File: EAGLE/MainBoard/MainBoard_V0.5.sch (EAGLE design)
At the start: 34 parts, among them IC2 CEM3340

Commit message: Renumber Parts
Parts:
- removed IC2: CEM3340, CEM:CEM3340
- removed J3: (no value), SparkFun-Connectors:CONN_08X2_SHROUD
- removed LINEAR-FM, PWM_C: WQP-PJ301M-12_JACK, thonkiconn:WQP-PJ301M-12_JACK
- removed R17: 20K, bourns:3386-W
- removed R18: 10K, bourns:3386-W
- removed R19, R20: 100K, rcl:R-US_0207/10
- added IC1: CEM3340, CEM:CEM3340
- added J8: (no value), SparkFun-Connectors:CONN_08X2_SHROUD
- added LIN_FM, PWM: WQP-PJ301M-12_JACK, thonkiconn:WQP-PJ301M-12_JACK
- added R13: 24KΩ, rcl:R-US_0207/10
- added R14: 1.8KΩ, rcl:R-US_0207/10
- added R5: 1MΩ, rcl:R-US_0207/10
- added R8: 10KΩ, rcl:R-US_0207/10
- C1, C3: value 0.01μF -> 0.001μF
- C4: value 1000pF -> 0.01μF
- C6: value 0.001μF -> 0.01μF
- CV2: SPICEPREFIX U -> (none)
- R1: value 1.8K -> 360KΩ
- R10: value 5.6K -> 5.6KΩ
- R11: value 600 -> 20KΩ; device rcl:R-US_0207/10 -> bourns:3386-W
- R12: value 10K -> 10KΩ; device rcl:R-US_0207/10 -> bourns:3386-W
- R15: value 470 -> 1.5MΩ
- R16: value 100K -> 470Ω
- R2: value 1.5M -> 100KΩ
- R3: value 360K -> 100KΩ
- R4: value 1M -> 100KΩ
- R6: value 1M -> 470Ω
- R7: value 470 -> 1MΩ
- R9: value 24K -> 600Ω
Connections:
- net +12V: now also IC1.16, J8.10, J8.9, R1.1, R15.1; no longer IC2.16, J3.10, J3.9, R2.1, R3.1
- net +5V: now also J8.11, J8.12; no longer J3.11, J3.12
- net -12V: now also J8.1, J8.2, R9.1; no longer J3.1, J3.2, R11.1
- net CV: now also J8.13, J8.14; no longer J3.13, J3.14
- net FCTL: now also IC1.15, R1.2, R2.1, R4.2, R6.1, R7.1; no longer IC2.15, R15.1, R16.1, R19.2, R20.2, R4.1
- net GATE: now also J8.15, J8.16; no longer J3.15, J3.16
- net GND: now also C5.2, C6.2, IC1.12, J8.3, J8.4, J8.5, J8.6, J8.7, J8.8, LIN_FM.1, PWM.1, R11.3, R14.1, R8.1; no longer C1.2, C3.2, IC2.12, J3.3, J3.4, J3.5, J3.6, J3.7, J3.8, LINEAR-FM.1, PWM_C.1, R1.1, R12.1, R17.3
- net HARD_S: now also C1.2, IC1.6; no longer C6.2, IC2.6
- net LIN_FM: now also IC1.13, R15.2, R16.1, R5.2; no longer IC2.13, R2.2, R6.2, R7.1
- net N$1: now also IC1.2; no longer IC2.2
- net N$10: now also R11.2, R7.2; no longer R17.2, R4.2
- net N$11: now also R12.3, R13.1; no longer R18.3, R9.1
- net N$13: now also IC1.7, R11.1; no longer IC2.7, R17.1
- net N$14: now also R2.2; no longer R16.2
- net N$15: now also IC1.3, R12.1, R12.2, R9.2; no longer IC2.3, R11.2, R18.1, R18.2
- net N$16: now also C1.1; no longer C6.1
- net N$2: now also C4.1, R6.2; no longer C1.1, R15.2
- net N$20: now also R3.1; no longer R19.1
- net N$22: now also R4.1; no longer R20.1
- net N$29: now also C3.2; no longer C5.2
- net N$3: now also IC1.14, R14.2; no longer IC2.14, R1.2
- net N$4: now also LIN_FM.2; no longer LINEAR-FM.2
- net N$5: now also R5.1; no longer R6.1
- net N$6: now also C6.1, R16.2; no longer C3.1, R7.2
- net N$7: now also C5.1, IC1.11; no longer C4.1, IC2.11
- net N$8: now also IC1.1, R13.2; no longer IC2.1, R9.2
- net PWM: now also IC1.5, PWM.2; no longer IC2.5, PWM_C.2
- net SAW: now also IC1.8; no longer IC2.8
- net SOFT_S: now also C3.1, IC1.9; no longer C5.1, IC2.9
- net SQUARE: now also IC1.4, R8.2; no longer IC2.4, R12.2
- net TRI: now also IC1.10; no longer IC2.10
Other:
- moved on the sheet: C1, C2, C3, C4, C5, C6, CV1, CV2, CV3, HARD_S, R1, R10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

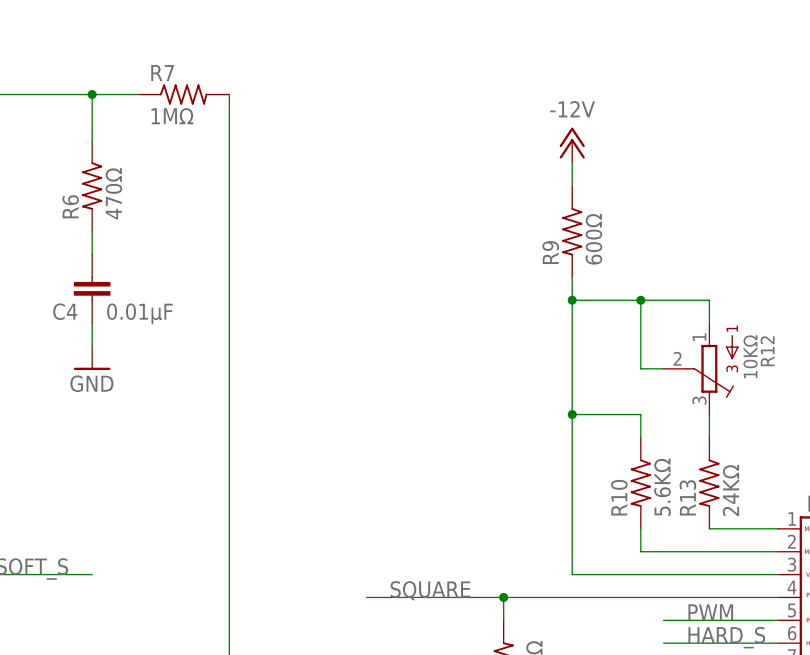
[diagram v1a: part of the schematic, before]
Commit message: Add 5V Reg. CAM Files
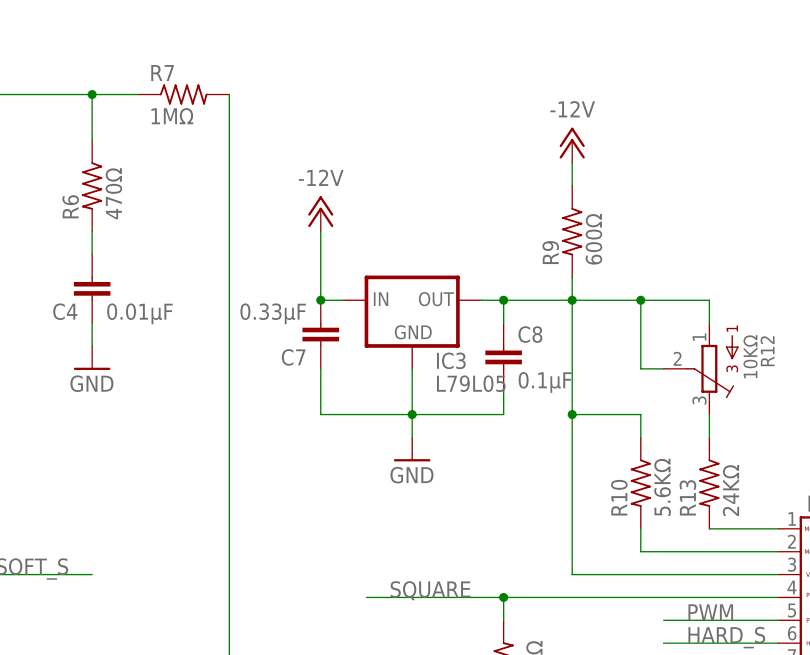
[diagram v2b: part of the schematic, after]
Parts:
- added C7: 0.33μF, rcl:C-EU050-025X075
- added C8: 0.1μF, rcl:C-EU050-025X075
- added IC3: L79L05, SparkFun-IC-Power:V_REG_78XXTO-92_UNTESTED
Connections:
- net -12V: now also C7.2, IC3.IN
- net GND: now also C7.1, C8.2, IC3.GND
- net N$15: now also C8.1, IC3.OUT
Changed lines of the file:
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@@
 <part name="CV2" library="thonkiconn" deviceset="WQP-PJ301M-12_JACK" device=""/>
 <part name="FRAME1" library="frames" library_urn="urn:adsk.eagle:library:229" deviceset="LETTER_L" device=""/>
+<part name="IC3" library="SparkFun-IC-Power" deviceset="V_REG_78XX" device="TO-92_UNTESTED" value="L79L05"/>
+<part name="P-4" library="supply1" library_urn="urn:adsk.eagle:library:371" deviceset="-12V" device=""/>
+<part name="C8" library="rcl" library_urn="urn:adsk.eagle:library:334" deviceset="C-EU" device="050-025X075" package3d_urn="urn:adsk.eagle:package:23637/1" value="0.1μF"/>
+<part name="C7" library="rcl" library_urn="urn:adsk.eagle:library:334" deviceset="C-EU" device="050-025X075" package3d_urn="urn:adsk.eagle:package:23637/1" value="0.33μF"/>
+<part name="GND18" library="supply1" library_urn="urn:adsk.eagle:library:371" deviceset="GND" device=""/>
 </parts>
 <sheets>
@@
 <attribute name="SHEET" x="233.68" y="1.27" size="2.54" layer="94"/>
 <attribute name="DRAWING_NAME" x="165.1" y="19.05" size="2.54" layer="94"/>
+</instance>
+<instance part="IC3" gate="G$1" x="111.76" y="124.46" smashed="yes">
+<attribute name="NAME" x="114.3" y="116.84" size="1.778" layer="95"/>
+<attribute name="VALUE" x="114.3" y="114.3" size="1.778" layer="96"/>
+</instance>
+<instance part="P-4" gate="1" x="101.6" y="134.62" smashed="yes" rot="R180">
+<attribute name="VALUE" x="99.06" y="137.16" size="1.778" layer="96"/>
+</instance>
+<instance part="C8" gate="G$1" x="121.92" y="119.38" smashed="yes">
+<attribute name="NAME" x="123.444" y="119.761" size="1.778" layer="95"/>
+<attribute name="VALUE" x="123.444" y="114.681" size="1.778" layer="96"/>
+</instance>
+<instance part="C7" gate="G$1" x="101.6" y="119.38" smashed="yes" rot="R180">
+<attribute name="NAME" x="100.076" y="118.999" size="1.778" layer="95" rot="R180"/>
+<attribute name="VALUE" x="100.076" y="124.079" size="1.778" layer="96" rot="R180"/>
+</instance>
+<instance part="GND18" gate="1" x="111.76" y="106.68" smashed="yes">
+<attribute name="VALUE" x="109.22" y="104.14" size="1.778" layer="96"/>
 </instance>
 </instances>
@@
 <pinref part="P-2" gate="1" pin="-12V"/>
 <wire x1="119.38" y1="22.86" x2="119.38" y2="25.4" width="0.1524" layer="91"/>
+</segment>
+<segment>
+<pinref part="P-4" gate="1" pin="-12V"/>
+<wire x1="101.6" y1="132.08" x2="101.6" y2="124.46" width="0.1524" layer="91"/>
+<pinref part="IC3" gate="G$1" pin="IN"/>
+<wire x1="101.6" y1="124.46" x2="104.14" y2="124.46" width="0.1524" layer="91"/>
+<pinref part="C7" gate="G$1" pin="2"/>
+<junction x="101.6" y="124.46"/>
 </segment>
 </net>
@@
 <wire x1="33.02" y1="127" x2="45.72" y2="127" width="0.1524" layer="91"/>
 </segment>
+<segment>
+<pinref part="IC3" gate="G$1" pin="GND"/>
+<wire x1="111.76" y1="116.84" x2="111.76" y2="111.76" width="0.1524" layer="91"/>
+<wire x1="101.6" y1="111.76" x2="111.76" y2="111.76" width="0.1524" layer="91"/>
+<wire x1="111.76" y1="111.76" x2="121.92" y2="111.76" width="0.1524" layer="91"/>
+<junction x="111.76" y="111.76"/>
+<pinref part="C8" gate="G$1" pin="2"/>
+<wire x1="121.92" y1="111.76" x2="121.92" y2="114.3" width="0.1524" layer="91"/>
+<pinref part="GND18" gate="1" pin="GND"/>
+<wire x1="111.76" y1="111.76" x2="111.76" y2="109.22" width="0.1524" layer="91"/>
+<pinref part="C7" gate="G$1" pin="1"/>
+<wire x1="101.6" y1="116.84" x2="101.6" y2="111.76" width="0.1524" layer="91"/>
+</segment>
 </net>
 <net name="N$16" class="0">
@@
 <pinref part="R12" gate="G$1" pin="2"/>
 <junction x="129.54" y="111.76"/>
-</segment>
-</net>
+<pinref part="IC3" gate="G$1" pin="OUT"/>
+<wire x1="119.38" y1="124.46" x2="121.92" y2="124.46" width="0.1524" layer="91"/>
+<pinref part="C8" gate="G$1" pin="1"/>
+<wire x1="121.92" y1="124.46" x2="129.54" y2="124.46" width="0.1524" layer="91"/>
+<wire x1="121.92" y1="121.92" x2="121.92" y2="124.46" width="0.1524" layer="91"/>
+<junction x="121.92" y="124.46"/>
+</segment>
+</net>

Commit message: Update Power IC Add Optional Component Clarification
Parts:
- IC3: device SparkFun-IC-Power:V_REG_78XXTO-92_UNTESTED -> SparkFun-IC-Power:V_REG_79LXX
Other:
- note added: "Place only R9 OR IC3, C7, & C8"
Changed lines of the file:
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@@
 <part name="CV2" library="thonkiconn" deviceset="WQP-PJ301M-12_JACK" device=""/>
 <part name="FRAME1" library="frames" library_urn="urn:adsk.eagle:library:229" deviceset="LETTER_L" device=""/>
-<part name="IC3" library="SparkFun-IC-Power" deviceset="V_REG_78XX" device="TO-92_UNTESTED" value="L79L05"/>
 <part name="P-4" library="supply1" library_urn="urn:adsk.eagle:library:371" deviceset="-12V" device=""/>
 <part name="C8" library="rcl" library_urn="urn:adsk.eagle:library:334" deviceset="C-EU" device="050-025X075" package3d_urn="urn:adsk.eagle:package:23637/1" value="0.1μF"/>
 <part name="C7" library="rcl" library_urn="urn:adsk.eagle:library:334" deviceset="C-EU" device="050-025X075" package3d_urn="urn:adsk.eagle:package:23637/1" value="0.33μF"/>
 <part name="GND18" library="supply1" library_urn="urn:adsk.eagle:library:371" deviceset="GND" device=""/>
+<part name="IC3" library="SparkFun-IC-Power" deviceset="V_REG_79LXX" device="" value="L79L05"/>
 </parts>
 <sheets>
 <sheet>
 <plain>
+<text x="114.3" y="134.62" size="1.778" layer="91" align="center">Place only R9
+OR
+IC3, C7, &amp; C8</text>
 </plain>
 <instances>
@@
 <attribute name="DRAWING_NAME" x="165.1" y="19.05" size="2.54" layer="94"/>
 </instance>
+<instance part="P-4" gate="1" x="101.6" y="134.62" smashed="yes" rot="R180">
+<attribute name="VALUE" x="99.06" y="137.16" size="1.778" layer="96"/>
+</instance>
+<instance part="C8" gate="G$1" x="121.92" y="119.38" smashed="yes">
+<attribute name="NAME" x="123.444" y="119.761" size="1.778" layer="95"/>
+<attribute name="VALUE" x="123.444" y="114.681" size="1.778" layer="96"/>
+</instance>
+<instance part="C7" gate="G$1" x="101.6" y="119.38" smashed="yes" rot="R180">
+<attribute name="NAME" x="100.076" y="118.999" size="1.778" layer="95" rot="R180"/>
+<attribute name="VALUE" x="100.076" y="124.079" size="1.778" layer="96" rot="R180"/>
+</instance>
+<instance part="GND18" gate="1" x="111.76" y="106.68" smashed="yes">
+<attribute name="VALUE" x="109.22" y="104.14" size="1.778" layer="96"/>
+</instance>
 <instance part="IC3" gate="G$1" x="111.76" y="124.46" smashed="yes">
 <attribute name="NAME" x="114.3" y="116.84" size="1.778" layer="95"/>
 <attribute name="VALUE" x="114.3" y="114.3" size="1.778" layer="96"/>
-</instance>
-<instance part="P-4" gate="1" x="101.6" y="134.62" smashed="yes" rot="R180">
-<attribute name="VALUE" x="99.06" y="137.16" size="1.778" layer="96"/>
-</instance>
-<instance part="C8" gate="G$1" x="121.92" y="119.38" smashed="yes">
-<attribute name="NAME" x="123.444" y="119.761" size="1.778" layer="95"/>
-<attribute name="VALUE" x="123.444" y="114.681" size="1.778" layer="96"/>
-</instance>
-<instance part="C7" gate="G$1" x="101.6" y="119.38" smashed="yes" rot="R180">
-<attribute name="NAME" x="100.076" y="118.999" size="1.778" layer="95" rot="R180"/>
-<attribute name="VALUE" x="100.076" y="124.079" size="1.778" layer="96" rot="R180"/>
-</instance>
-<instance part="GND18" gate="1" x="111.76" y="106.68" smashed="yes">
-<attribute name="VALUE" x="109.22" y="104.14" size="1.778" layer="96"/>
 </instance>
 </instances>
@@
 <pinref part="P-4" gate="1" pin="-12V"/>
 <wire x1="101.6" y1="132.08" x2="101.6" y2="124.46" width="0.1524" layer="91"/>
-<pinref part="IC3" gate="G$1" pin="IN"/>
 <wire x1="101.6" y1="124.46" x2="104.14" y2="124.46" width="0.1524" layer="91"/>
 <pinref part="C7" gate="G$1" pin="2"/>
 <junction x="101.6" y="124.46"/>
+<pinref part="IC3" gate="G$1" pin="IN"/>
 </segment>
 </net>
@@
 </segment>
 <segment>
-<pinref part="IC3" gate="G$1" pin="GND"/>
 <wire x1="111.76" y1="116.84" x2="111.76" y2="111.76" width="0.1524" layer="91"/>
 <wire x1="101.6" y1="111.76" x2="111.76" y2="111.76" width="0.1524" layer="91"/>
@@
 <pinref part="C7" gate="G$1" pin="1"/>
 <wire x1="101.6" y1="116.84" x2="101.6" y2="111.76" width="0.1524" layer="91"/>
+<pinref part="IC3" gate="G$1" pin="GND"/>
 </segment>
 </net>
@@
 <pinref part="R12" gate="G$1" pin="2"/>
 <junction x="129.54" y="111.76"/>
-<pinref part="IC3" gate="G$1" pin="OUT"/>
 <wire x1="119.38" y1="124.46" x2="121.92" y2="124.46" width="0.1524" layer="91"/>
 <pinref part="C8" gate="G$1" pin="1"/>
@@
 <wire x1="121.92" y1="121.92" x2="121.92" y2="124.46" width="0.1524" layer="91"/>
 <junction x="121.92" y="124.46"/>
+<pinref part="IC3" gate="G$1" pin="OUT"/>
 </segment>
 </net>
@@
 </drawing>
 <compatibility>
+<note version="6.3" minversion="6.2.2" severity="warning">
+Since Version 6.2.2 text objects can contain more than one line,
+which will not be processed correctly with this version.
+</note>
 <note version="8.2" severity="warning">
 Since Version 8.2, EAGLE supports online libraries. The ids
